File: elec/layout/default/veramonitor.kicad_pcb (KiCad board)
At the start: 2 copper layers, 111.2 x 70.4 mm, 109 parts, among them J1 ?, U1 ?, U10 ?, U11 ?, U12 ?, U13 ?, U14 ?, U15 ?, U16 ?, U17 ?, U18 ?, U19 ?, U2 ?, U20 ?, U21 ?, U22 ?, U23 ?, U24 ?, U25 ?, U26 ?, U27 ?, U28 ?, U29 ?, U3 ?, U30 ?, U31 ?, U32 ?, U33 ?, U34 ?, U35 ?, U36 ?, U37 ?, U38 ?, U39 ?, U4 ?, U40 ?, U41 ?, U42 ?, U43 ?, U44 ?, U45 ?, U46 ?, U47 ?, U48 ?, U49 ?, U5 ?, U50 ?, U51 ?, U6 ?, U7 ?, U8 ?, U9 ?

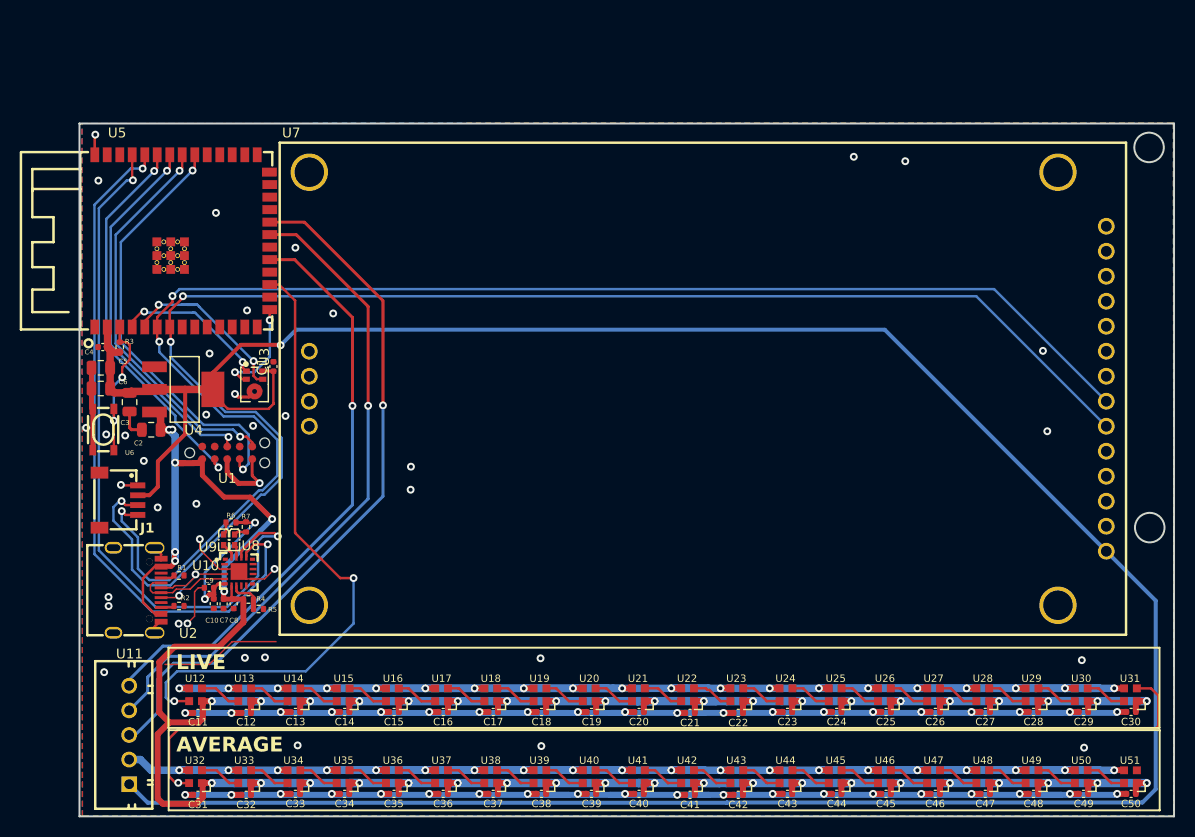
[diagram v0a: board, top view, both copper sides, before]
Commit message: removed usb-uart
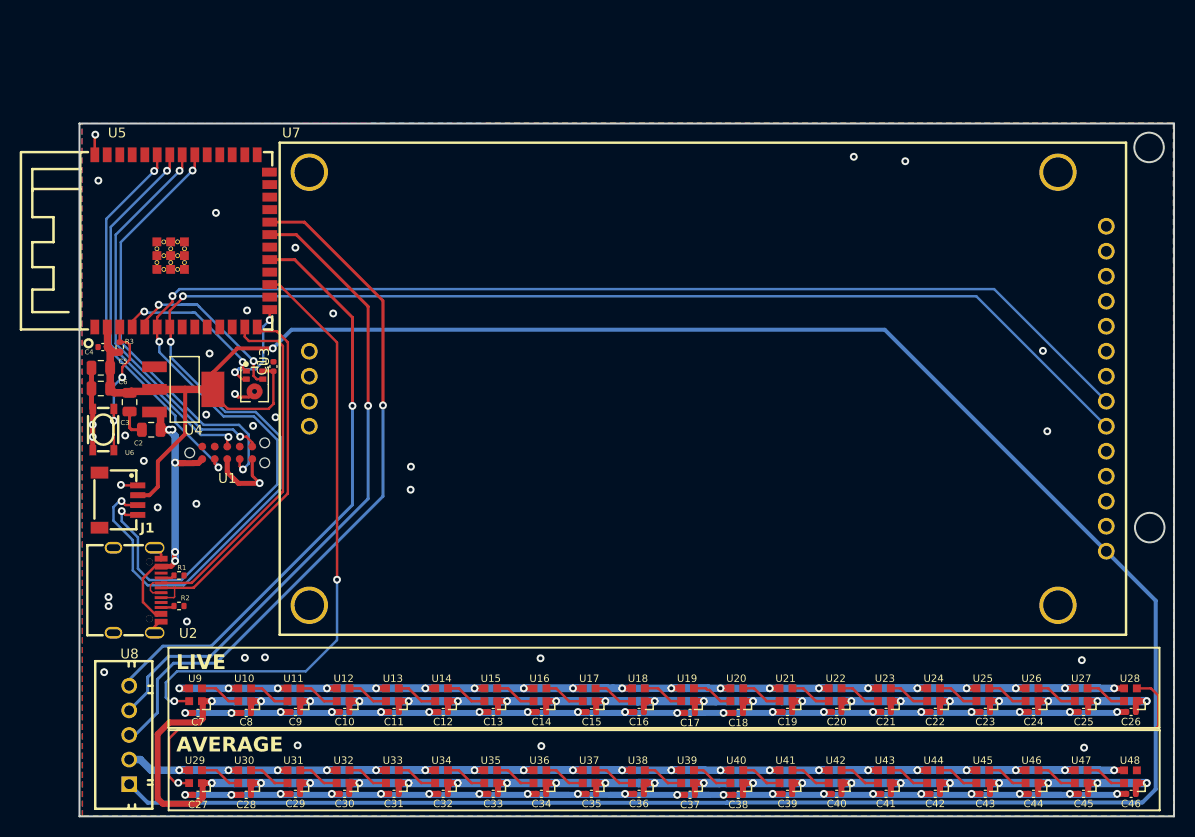
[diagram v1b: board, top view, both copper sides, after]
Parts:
- removed the C10 at (53.7, 115.7)
- removed the C7 at (54.7, 115.7)
- removed the C8 at (55.8, 115.7)
- removed the C9 at (53.2, 114.1)
- removed R4, R6, R7: 62.5mW Thick Film Resistors 50V ±100ppm/℃ ±1% 20kΩ 0402 Chi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, lib:R0402
- removed R5: 62.5mW Thick Film Resistors 50V ±100ppm/℃ ±1% 51kΩ 0402 Chi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, lib:R0402
- removed the U10 at (56.3, 112.4)
- removed the U8 at (55.9, 109.2)
- removed the U9 at (54.7, 109.2)
- renumbered C14 to C10, C15 to C11, C16 to C12, C17 to C13, C18 to C14, C19 to C15, C20 to C16, C21 to C17, C22 to C18, C23 to C19, C24 to C20, C25 to C21, C26 to C22, C27 to C23, C28 to C24, C29 to C25, C30 to C26, C31 to C27, C32 to C28, C33 to C29, C34 to C30, C35 to C31, C36 to C32, C37 to C33, C38 to C34, C39 to C35, C40 to C36, C41 to C37, C42 to C38, C43 to C39, C44 to C40, C45 to C41, C46 to C42, C47 to C43, C48 to C44, C49 to C45, C50 to C46, C11 to C7, C12 to C8, C13 to C9, U13 to U10, U14 to U11, U15 to U12, U16 to U13, U17 to U14, U18 to U15, U19 to U16, U20 to U17, U21 to U18, U22 to U19, U23 to U20, U24 to U21, U25 to U22, U26 to U23, U27 to U24, U28 to U25, U29 to U26, U30 to U27, U31 to U28, U32 to U29, U33 to U30, U34 to U31, U35 to U32, U36 to U33, U37 to U34, U38 to U35, U39 to U36, U40 to U37, U41 to U38, U42 to U39, U43 to U40, U44 to U41, U45 to U42, U46 to U43, U47 to U44, U48 to U45, U49 to U46, U50 to U47, U51 to U48, U11 to U8, U12 to U9
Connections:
- net lcd-nc renamed nc
- U5 pad 13: io19 -> dm
- U5 pad 14: io20 -> dp
- U5 pad 36: rx -> rxd0
- U5 pad 37: tx -> txd0
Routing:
- net tx: track 72.9 -> 0.00 mm, vias 2 -> 0
- net rx: track 71.0 -> 0.00 mm, vias 2 -> 0
- net vcc: track 413.9 -> 370.6 mm, vias 47 -> 45
- net dm: track 9.93 -> 39.2 mm
- net dp: track 12.1 -> 38.3 mm, vias 2 -> 0
- net vdd: track 16.2 -> 0.00 mm, vias 2 -> 0
- net gnd: track 689.4 -> 674.4 mm, vias 118 -> 115
- net (no net): track 12.2 -> 0.00 mm
- net vbus: track 3.79 -> 0.00 mm
- net led_data: track 64.9 -> 62.7 mm
- net gpio_period_2_slash_txt: track 1.57 -> 0.00 mm
- net uart_converter.r_tx_led-anode: track 1.32 -> 0.00 mm
- net gpio_period_3_slash_rxt: track 1.30 -> 0.00 mm
- net uart_converter.r_rx_led-anode: track 1.26 -> 0.00 mm
- net sda: track 155.2 -> 155.8 mm
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
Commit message: edits
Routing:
- net vcc: track 370.6 -> 386.7 mm
- net gnd: track 674.4 -> 680.5 mm, vias 115 -> 117
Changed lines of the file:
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@@
 	)
 	(segment
+		(start 47.725 118.325)
+		(end 48.375 117.675)
+		(width 0.25)
+		(layer "F.Cu")
+		(net 1)
+	)
+	(segment
 		(start 41.3 95.77)
 		(end 41.43 95.9)
@@
 	)
 	(segment
+		(start 50.7075 112.825)
+		(end 50.7075 111.7925)
+		(width 0.25)
+		(layer "F.Cu")
+		(net 1)
+	)
+	(segment
+		(start 50.7075 111.7925)
+		(end 51.25 111.25)
+		(width 0.25)
+		(layer "F.Cu")
+		(net 1)
+	)
+	(segment
 		(start 111.54 135.015)
 		(end 110.52 135.015)
@@
 	)
 	(segment
+		(start 47.725 118.645)
+		(end 47.725 118.325)
+		(width 0.25)
+		(layer "F.Cu")
+		(net 1)
+	)
+	(segment
 		(start 81.645 126.695)
 		(end 80.725 126.695)
@@
 	)
 	(segment
+		(start 48.925 117.675)
+		(end 49.5 118.25)
+		(width 0.25)
+		(layer "F.Cu")
+		(net 1)
+	)
+	(segment
 		(start 41.63 68.09)
 		(end 41.63 70.075)
@@
 	)
 	(segment
+		(start 50.7075 117.2075)
+		(end 51 117.5)
+		(width 0.25)
+		(layer "F.Cu")
+		(net 1)
+	)
+	(segment
 		(start 146.22 124.29)
 		(end 145.22 124.29)
@@
 	)
 	(segment
+		(start 50.7075 115.925)
+		(end 50.7075 117.2075)
+		(width 0.25)
+		(layer "F.Cu")
+		(net 1)
+	)
+	(segment
 		(start 51.225 124.295)
 		(end 50.225 124.295)
@@
 	)
 	(segment
+		(start 48.375 117.675)
+		(end 48.925 117.675)
+		(width 0.25)
+		(layer "F.Cu")
+		(net 1)
+	)
+	(segment
 		(start 121.56 135.015)
 		(end 120.72 135.015)
@@
 	)
 	(via
+		(at 49.5 118.25)
+		(size 0.8)
+		(drill 0.4)
+		(layers "F.Cu" "B.Cu")
+		(net 1)
+	)
+	(via
 		(at 145.22 124.29)
 		(size 0.8)
@@
 	)
 	(via
+		(at 51.25 111.25)
+		(size 0.8)
+		(drill 0.4)
+		(layers "F.Cu" "B.Cu")
+		(net 1)
+	)
+	(via
 		(at 145.52 126.69)
 		(size 0.8)
@@
 	)
 	(segment
+		(start 47.873133 116.875)
+		(end 48.365 116.875)
+		(width 0.254)
+		(layer "F.Cu")
+		(net 35)
+	)
+	(segment
 		(start 72.525 125.595)
 		(end 73.525 125.595)
@@
 	)
 	(segment
-		(start 47.873133 116.875)
-		(end 48.365 116.875)
-		(width 0.254)
+		(start 82.605 125.675)
+		(end 82.525 125.595)
+		(width 0.6096)
 		(layer "F.Cu")
 		(net 35)
 	)
 	(segment
-		(start 82.605 125.675)
-		(end 82.525 125.595)
+		(start 46 113.648133)
+		(end 46.53 113.118133)
 		(width 0.6096)
 		(layer "F.Cu")
@@
 	)
 	(segment
-		(start 46.53 113.118133)
-		(end 46.53 115.531867)
-		(width 0.254)
-		(layer "F.Cu")
-		(net 35)
-	)
-	(segment
 		(start 49.3375 111.775)
 		(end 49.375 111.775)
@@
 	)
 	(segment
+		(start 46 116.25)
+		(end 46.238 116.488)
+		(width 0.254)
+		(layer "F.Cu")
+		(net 35)
+	)
+	(segment
 		(start 77.52 135.015)
 		(end 77.52 133.915)
@@
 	)
 	(segment
+		(start 46 122)
+		(end 46 114.148133)
+		(width 0.6096)
+		(layer "F.Cu")
+		(net 35)
+	)
+	(segment
 		(start 107.5 133.935)
 		(end 107.52 133.915)
@@
 	)
 	(segment
+		(start 47.75 123.75)
+		(end 46 122)
+		(width 0.6096)
+		(layer "F.Cu")
+		(net 35)
+	)
+	(segment
 		(start 142.58 126.69)
 		(end 142.58 125.65)
@@
 	)
 	(segment
+		(start 46 114.148133)
+		(end 46 113.648133)
+		(width 0.6096)
+		(layer "F.Cu")
+		(net 35)
+	)
+	(segment
+		(start 47.486133 116.488)
+		(end 47.873133 116.875)
+		(width 0.254)
+		(layer "F.Cu")
+		(net 35)
+	)
+	(segment
 		(start 57.5 135.115)
 		(end 57.5 133.935)
@@
 	)
 	(segment
+		(start 46 114.148133)
+		(end 46 116.25)
+		(width 0.254)
+		(layer "F.Cu")
+		(net 35)
+	)
+	(segment
 		(start 102.6 126.79)
 		(end 102.6 125.67)
@@
 	)
 	(segment
+		(start 46.238 116.488)
+		(end 47.486133 116.488)
+		(width 0.254)
+		(layer "F.Cu")
+		(net 35)
+	)
+	(segment
 		(start 49.8601 101.4101)
 		(end 49.8 101.35)
@@
 	)
 	(segment
-		(start 46.53 115.531867)
-		(end 47.873133 116.875)
-		(width 0.254)
-		(layer "F.Cu")
-		(net 35)
-	)
-	(segment
 		(start 147.52 133.915)
 		(end 148.52 133.915)
@@
 	)
 	(segment
+		(start 49.21 127.76)
+		(end 47.75 126.3)
+		(width 0.6096)
+		(layer "F.Cu")
+		(net 35)
+	)
+	(segment
 		(start 147.52 125.59)
 		(end 148.52 125.59)
@@
 		(layer "F.Cu")
 		(net 35)
+	)
+	(segment
+		(start 47.75 126.3)
+		(end 47.75 123.75)
+		(width 0.6096)
+		(layer "F.Cu")
+		(net 35)

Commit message: edits
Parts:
- removed C15, C16, C17, C18, C19, C20, C21, C22, C23, C24, C25, C26, C27, C28, C29, C30, C31, C32, C33, C34, C35, C36, C37, C38, C39, C40, C41, C42, C43, C44, C45, C46: 16V 100nF X7R ±10% 0402 Multilayer Ceramic Capacitors MLCC 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, lib:C0402
- removed U22, U23, U24, U25, U26, U27, U28, U29, U30, U31, U32, U33, U34, U35, U36, U37, U38, U39, U40, U41, U42, U43, U44, U45, U46, U47, U48: ?, lib:LED-SMD_4P-L2.0-W2.0-BR
- added R10: 50mW Thick Film Resistors 25V ±1% ±200ppm/℃ 10kΩ 0201 Chip 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, lib:R0201, F.Cu at (126.0, 76.3)
- added R4: 62.5mW Thick Film Resistors 50V ±100ppm/℃ ±1% 10kΩ 0402 Chi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, lib:R0402, F.Cu at (57.7, 98.8)
- added R5: 50mW Thick Film Resistors 25V ±1% ±200ppm/℃ 10kΩ 0201 Chip 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, lib:R0201, F.Cu at (71.7, 111.6)
- added R6: 50mW Thick Film Resistors 25V ±1% ±200ppm/℃ 10kΩ 0201 Chip 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, lib:R0201, F.Cu at (89.7, 111.8)
- added R7: 50mW Thick Film Resistors 25V ±1% ±200ppm/℃ 10kΩ 0201 Chip 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, lib:R0201, F.Cu at (107.8, 111.8)
- added R8: 50mW Thick Film Resistors 25V ±1% ±200ppm/℃ 10kΩ 0201 Chip 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, lib:R0201, F.Cu at (126.0, 111.7)
- added R9: 50mW Thick Film Resistors 25V ±1% ±200ppm/℃ 10kΩ 0201 Chip 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, lib:R0201, F.Cu at (125.9, 95.0)
- C7: value 16V 100nF X7R ±10% 0402 Multilayer Ceramic Capacitors MLCC - SMD/SMT ROHS -> 6.3V 10uF X5R ±20% 0402 Multilayer Ceramic Capacitors MLCC - SMD/SMT ROHS
- U10, U12, U14, U16, U18, U20: footprint lib:LED-SMD_4P-L2.0-W2.0-BR -> lib:KEY-TH_CPG1511F01S0X
- U21: footprint lib:LED-SMD_4P-L2.0-W2.0-BR -> lib:BUZ-SMD_4P-L13.0-W13.0-P11.4-BL
- U7: footprint lib:COMM-TH_HS12864G18B -> lib:LCD-TH_L56.5-W34.0_1-8INCH-LCD-MODULE
- U8: footprint lib:CONN-TH_5P-P2.50_XH-5A_C2318 -> lib:TQFN-16_L3.0-W3.0-P0.50-BL-EP1.5
- moved C14 63.7 mm to (134.2, 83.9), turned to 0 degrees
- moved U20 59.8 mm to (133.8, 71.5)
- moved C13 57.7 mm to (134.3, 102.0), turned to 0 degrees
- moved C12 57.6 mm to (134.2, 120.0), turned to 0 degrees
- moved U19 55.2 mm to (134.3, 80.3), turned to -90 degrees
- moved U15 53.2 mm to (134.4, 116.5), turned to -90 degrees
- moved U21 52.1 mm to (61.5, 111.5)
- moved U18 51.0 mm to (133.6, 89.7)
- moved U17 50.2 mm to (134.5, 98.4), turned to -90 degrees
- moved U16 49.8 mm to (133.6, 107.7)
- moved U13 45.1 mm to (116.2, 116.8), turned to -90 degrees
- moved C11 44.8 mm to (116.3, 120.2), turned to 0 degrees
- moved U14 42.4 mm to (115.6, 107.8)
- moved U7 37.8 mm to (68.0, 82.2), turned to -90 degrees
- moved U11 37.5 mm to (98.4, 116.4), turned to -90 degrees
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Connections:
- net reset renamed jtag_connector-reset
- C10 pad 1: vcc -> vcc-1
- C11 pad 1: vcc -> vcc-1
- C12 pad 1: vcc -> vcc-1
- C13 pad 1: vcc -> vcc-1
- C14 pad 1: vcc -> vcc-1
- C7 pad 1: vcc -> vcc-1
- C8 pad 1: vcc -> vcc-1
- C9 pad 1: vcc -> vcc-1
- U10 pad 1: vcc -> sw1-key
- U10 pad 2: ledrow1.led2.ic-vcc -> gnd
- U11 pad 1: vcc -> vcc-1
- U11 pad 2: ledrow1.led3.ic-vcc -> sw2-dout
- U11 pad 4: ledrow1.led2.ic-vcc -> sw1-dout
- U12 pad 1: vcc -> sw2-key
- U12 pad 2: ledrow1.led4.ic-vcc -> gnd
- U13 pad 1: vcc -> vcc-1
- U13 pad 2: ledrow1.led5.ic-vcc -> sw3-dout
- U13 pad 4: ledrow1.led4.ic-vcc -> sw2-dout
- U14 pad 1: vcc -> sw3-key
- U14 pad 2: ledrow1.led6.ic-vcc -> gnd
- U15 pad 1: vcc -> vcc-1
- U15 pad 2: ledrow1.led7.ic-vcc -> sw4-dout
- U15 pad 4: ledrow1.led6.ic-vcc -> sw3-dout
- U16 pad 1: vcc -> sw4-key
- U16 pad 2: ledrow1.led8.ic-vcc -> gnd
- U17 pad 1: vcc -> vcc-1
- U17 pad 2: ledrow1.led9.ic-vcc -> sw5-dout
- U17 pad 4: ledrow1.led8.ic-vcc -> sw4-dout
- U18 pad 1: vcc -> sw5-key
- U18 pad 2: ledrow1-dout -> gnd
- U19 pad 1: vcc -> vcc-1
- U19 pad 2: ledrow2.led1.ic-vcc -> sw6-dout
- U19 pad 4: ledrow1-dout -> sw5-dout
- U20 pad 1: vcc -> sw6-key
- U20 pad 2: ledrow2.led2.ic-vcc -> gnd
- U21 pad 1: vcc -> outp
- U21 pad 2: ledrow2.led3.ic-vcc -> outn
- U21 pad 3: gnd -> dummy
- U21 pad 4: ledrow2.led2.ic-vcc -> dummy
- U5 pad 10: io17 -> din
- U5 pad 11: io18 -> bclk
- U5 pad 12: io8 -> lrclk
- U5 pad 16: io46 -> backlighten
- U5 pad 17: led_data -> micro.ic-reset
- U5 pad 18: io10 -> dc
- U5 pad 19: p5 -> cs
- U5 pad 20: io12 -> sck
- U5 pad 21: p4 -> mosi
- U5 pad 22: p3 -> io14
- U7 pad 1: vcc-1 -> vcc
- U7 pad 3: cs -> mosi
- U7 pad 4: rst -> sck
- U7 pad 5: a0 -> cs
- U7 pad 6: sda -> dc
- U7 pad 7: scl -> micro.ic-reset
- U7 pad 8: led -> backlighten
- U8 pad 1: vcc-1 -> din
- U8 pad 2: gnd -> gain_slot
- U8 pad 3: p3 -> gnd
- U8 pad 4: p4 -> sd_mode_hash
- U8 pad 5: p5 -> n_period_c_period
- U9 pad 1: vcc -> vcc-1
- U9 pad 2: ledrow1.led1.ic-vcc -> sw1-dout
- U9 pad 4: led_data -> io16
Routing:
- net gnd: track 680.5 -> 36.0 mm, vias 117 -> 39
- net vcc: track 386.7 -> 103.0 mm, vias 45 -> 4
- net sda: track 155.8 -> 20.2 mm, vias 3 -> 2
- net scl: track 153.5 -> 22.3 mm, vias 3 -> 2
- net ledrow2-dout: track 112.8 -> 0.00 mm, vias 1 -> 0
- net p3: track 72.5 -> 0.00 mm, vias 1 -> 0
- net p4: track 66.6 -> 0.00 mm, vias 1 -> 0
- net led_data: track 62.7 -> 0.00 mm, vias 2 -> 0
- net p5: track 60.5 -> 0.00 mm, vias 1 -> 0
- net io16: track 0.00 -> 48.9 mm, vias 0 -> 2
- net tck: track 44.0 -> 5.86 mm, vias 2 -> 0
- net tms: track 39.9 -> 5.34 mm, vias 2 -> 0
- net tdo: track 40.4 -> 8.31 mm
- net tdi: track 38.8 -> 8.84 mm
- net lrclk: track 0.00 -> 21.3 mm
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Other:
- board size 111.2 x 70.4 mm -> 105.2 x 61.6 mm
- board text removed: "AVERAGE"
- board text removed: "LIVE"

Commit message: added keys
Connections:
- R10 pad 2: sw6-key -> io35
- R5 pad 2: sw1-key -> io14
- R6 pad 2: sw2-key -> io21
- R7 pad 2: sw3-key -> io47
- R8 pad 2: sw4-key -> io48
- R9 pad 2: sw5-key -> io45
- U10 pad 1: sw1-key -> io14
- U12 pad 1: sw2-key -> io21
- U14 pad 1: sw3-key -> io47
- U16 pad 1: sw4-key -> io48
- U18 pad 1: sw5-key -> io45
- U20 pad 1: sw6-key -> io35
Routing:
- net io48: track 0.00 -> 94.0 mm, vias 0 -> 1
- net io45: track 0.00 -> 92.1 mm, vias 0 -> 1
- net io35: track 0.00 -> 86.8 mm, vias 0 -> 1
- net io47: track 0.00 -> 76.3 mm, vias 0 -> 1
- net io21: track 0.00 -> 67.2 mm, vias 0 -> 1
- net io14: track 0.00 -> 58.1 mm, vias 0 -> 1
- net vcc-1: track 284.5 -> 325.5 mm
- net sw4-dout: track 0.00 -> 24.6 mm, vias 0 -> 2
- net sw5-dout: track 0.00 -> 24.5 mm, vias 0 -> 2
- net sw3-dout: track 0.00 -> 17.5 mm, vias 0 -> 2
- net sw1-dout: track 0.00 -> 17.5 mm, vias 0 -> 2
- net sw2-dout: track 0.00 -> 16.9 mm, vias 0 -> 2
- net sw5-key: track 6.43 -> 0.00 mm
- net sw6-key: track 6.05 -> 0.00 mm
- net sw2-key: track 5.74 -> 0.00 mm
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
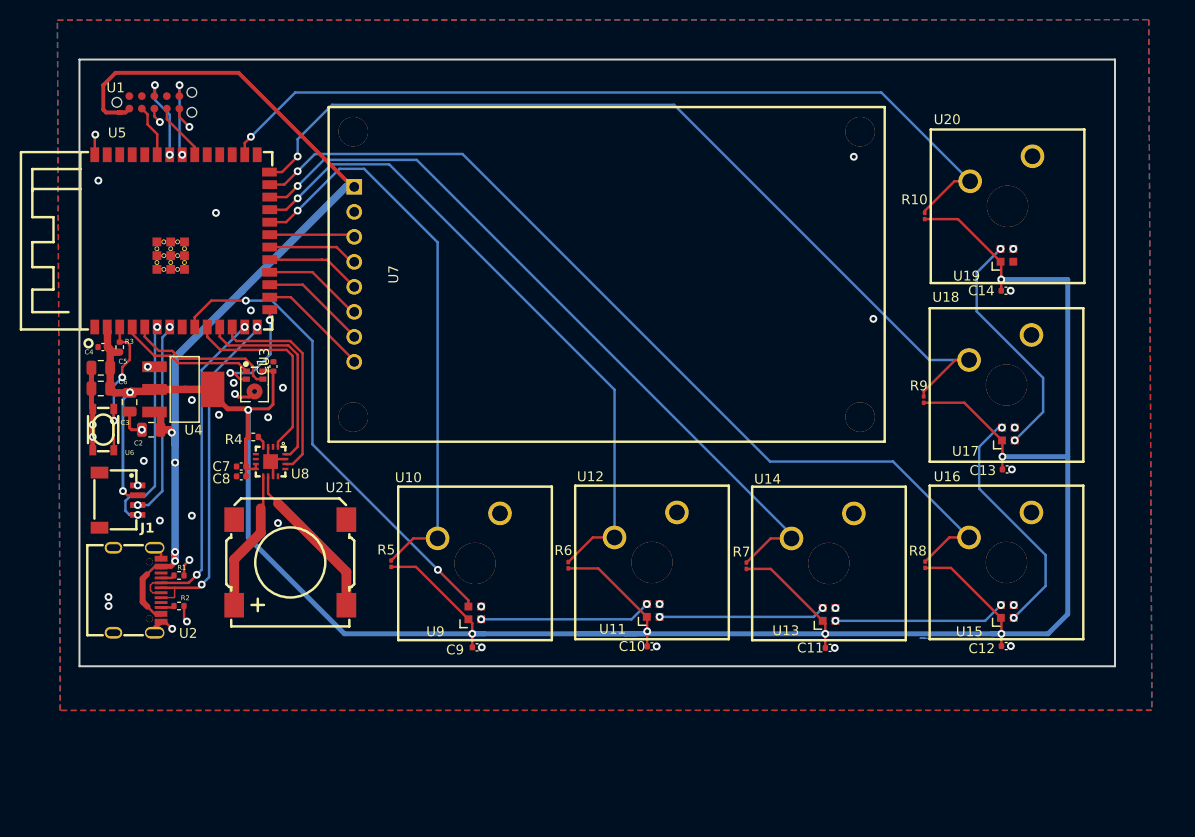
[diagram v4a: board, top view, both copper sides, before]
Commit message: checking DFM
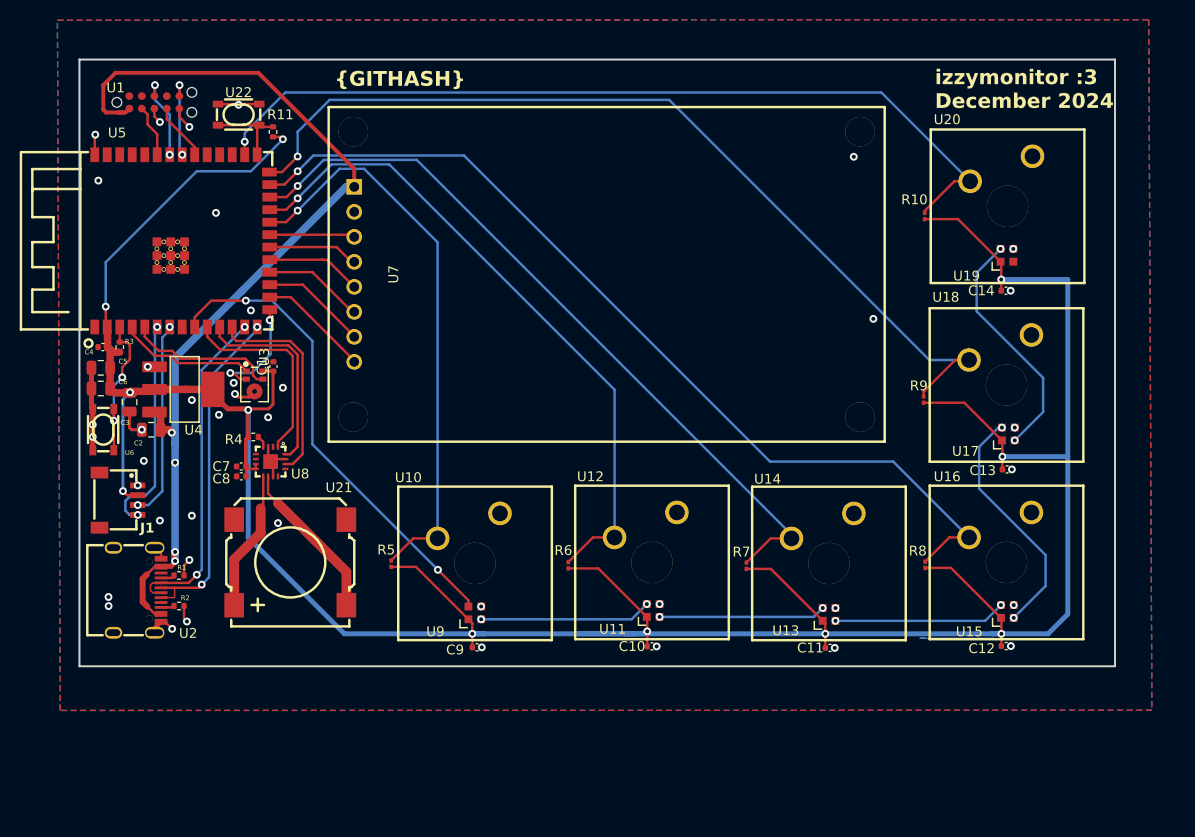
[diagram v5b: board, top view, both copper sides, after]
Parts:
- added R11: 62.5mW Thick Film Resistors 50V ±100ppm/℃ ±1% 10kΩ 0402 Chi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, lib:R0402, F.Cu at (59.8, 67.8)
- added U22: ?, lib:KEY-SMD_4P-L4.2-W3.2-P2.20-LS4.6, F.Cu at (56.2, 66.0)
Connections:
- U5 pad 27: io0 -> micro.ic-vcc
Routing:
- net vcc-1: track 325.5 -> 356.5 mm, vias 9 -> 11
- net micro.ic-vcc: track 0.00 -> 8.76 mm
- net gnd: track 36.0 -> 40.5 mm, vias 39 -> 40
- net vcc: track 102.0 -> 103.1 mm
- net io45: track 92.1 -> 93.0 mm
- net io35: track 86.8 -> 87.4 mm
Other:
- board text added: "izzymonitor :3 December 2024"
- board text added: "{GITHASH}"

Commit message: rerun
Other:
- board text removed: "{GITHASH}"
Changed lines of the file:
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@@
 		(at 56.25 66 180)
 		(property "Reference" "U22"
-			(at 0 2.25 360)
+			(at 0 2.25 0)
 			(layer "F.SilkS")
 			(effects
@@
 		)
 		(property "Value" "?"
-			(at 0 5.07 360)
+			(at 0 5.07 0)
 			(layer "F.Fab")
 			(effects
@@
 		)
 		(property "Footprint" ""
-			(at 0 0 360)
+			(at 0 0 0)
 			(layer "F.Fab")
 			(hide yes)
@@
 		)
 		(property "Datasheet" ""
-			(at 0 0 360)
+			(at 0 0 0)
 			(layer "F.Fab")
 			(hide yes)
@@
 		)
 		(property "Description" ""
-			(at 0 0 360)
+			(at 0 0 0)
 			(layer "F.Fab")
 			(hide yes)
@@
 		)
 		(fp_text user "${REFERENCE}"
-			(at 0 0 360)
+			(at 0 0 0)
 			(layer "F.Fab")
 			(effects
@@
 		(layer "Edge.Cuts")
 	)
-	(gr_text "{GITHASH}"
-		(at 66 63.25 0)
-		(layer "F.SilkS")
-		(effects
-			(font
-				(size 1.5 1.5)
-				(thickness 0.3)
-				(bold yes)
-			)
-			(justify left bottom)
-		)
-	)
 	(gr_text "izzymonitor :3\nDecember 2024"
